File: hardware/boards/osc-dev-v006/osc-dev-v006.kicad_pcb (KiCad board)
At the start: 6 copper layers, 50 x 40 mm, 87 parts, among them J1 JST-PH-H, J10 TTL-JST, J2 LINKE, J3 Qwiic, J4 MOT, J5 POS, J6 ENC, J7 NTC, J8 TTL, J9 TTL-JST, U1 HT7533-1, U2 CH32V006F8P6, U3 DRV8212PDSGR

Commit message: board: v006 rev-2a schematic refresh, family designators, terminal bias, tier-2 position input
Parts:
- renumbered C13 to Ca1, C6 to Ch1, C7 to Ch2, C8 to Ch3, C9 to Ch4, Cin1 to Ci1, C1 to Cp1, C2 to Cp2, C3 to Cp3, C4 to Cu1, C5 to Cu2, LED1 to Dl1, LED2 to Dl2, D4 to Dl3, D5 to Dl4, D1 to Dp1, D2 to Dp2, D6 to Dx1, R21 to Ra1, R14 to Rh1, R1 to Rl1, R2 to Rl2, R4 to Rl3, R8 to Rl4, R22 to Rn1, R12 to Rq1, R13 to Rq2, R10 to Rq3, R11 to Rq4, RS1 to Rs1, RS2 to Rs2, R7 to Ru1, R23 to Rx1, R24 to Rx2

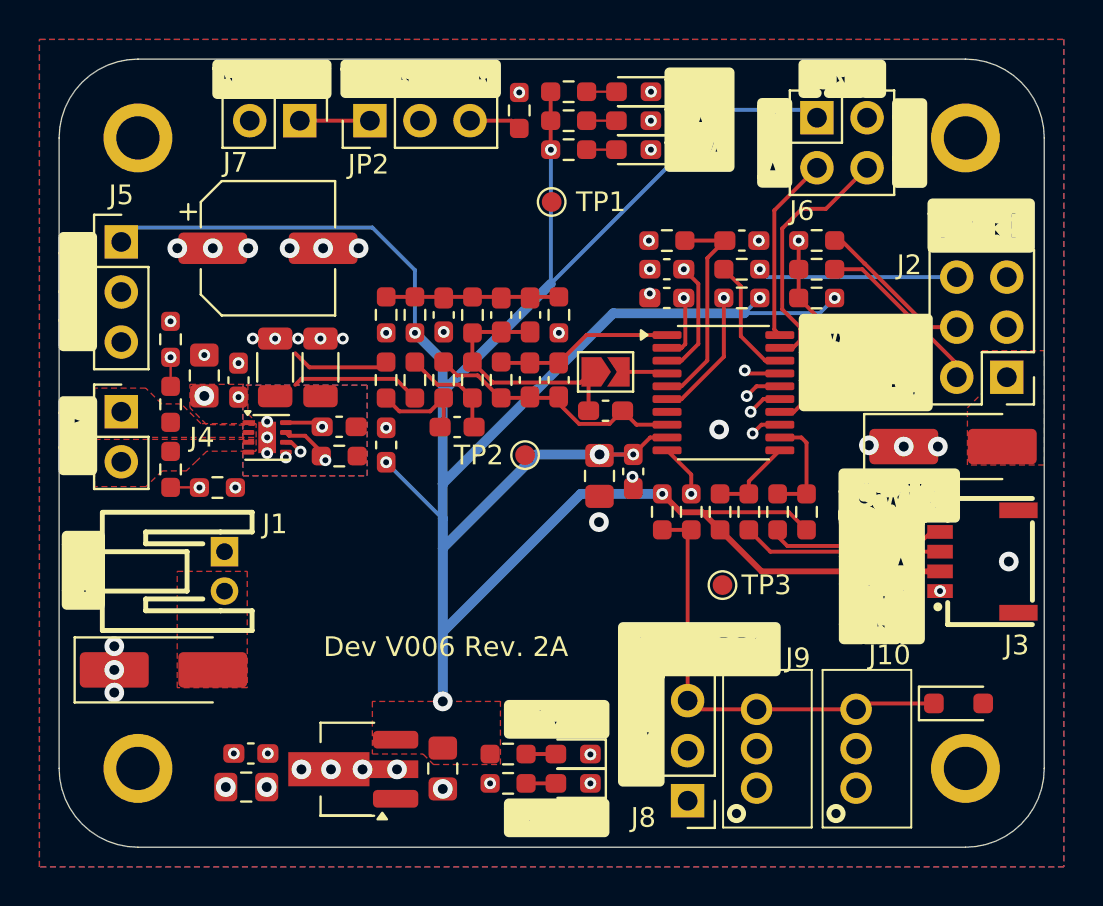
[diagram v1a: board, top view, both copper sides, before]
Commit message: board: v006 rev-2a placement, silk labels, test point rows, silk rules
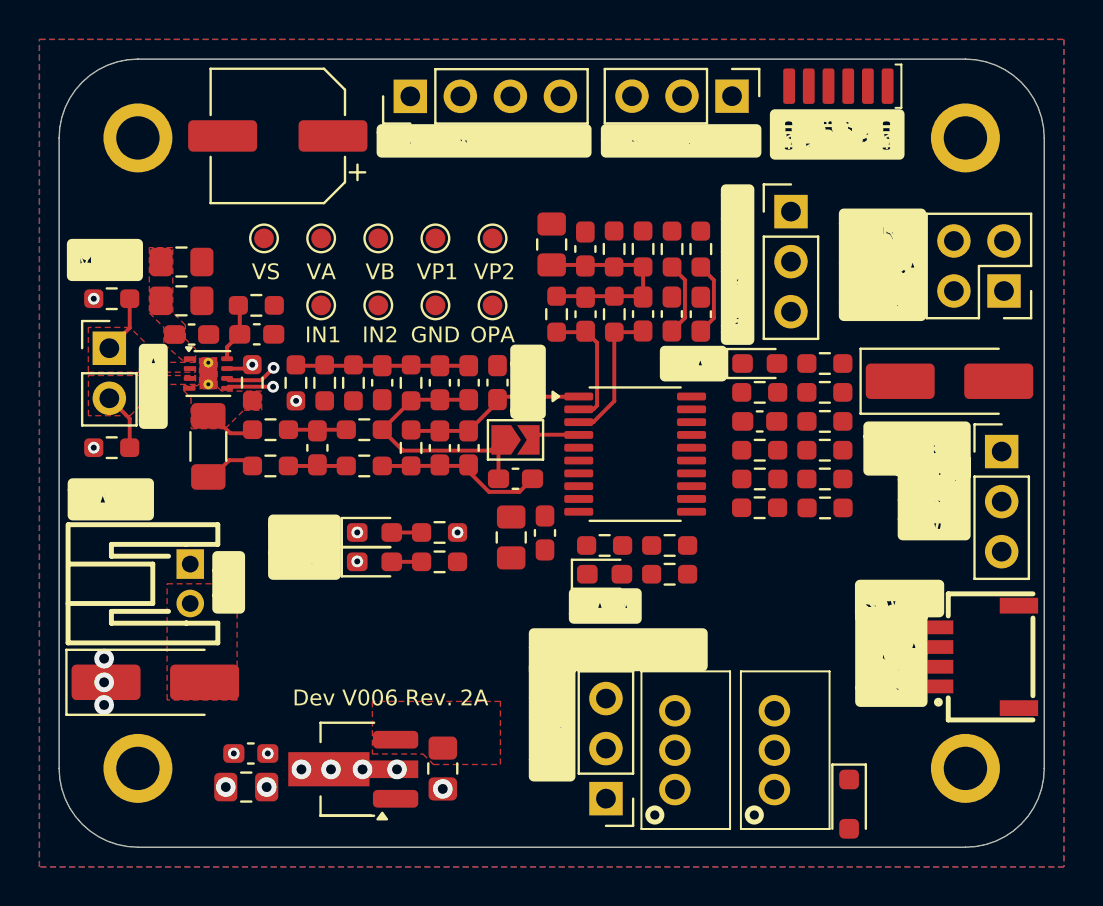
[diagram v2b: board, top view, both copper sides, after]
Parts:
- removed D3: BLUE, LED_SMD:LED_0603_1608Metric_Pad1.05x0.95mm_HandSolder
- removed FB1: 600Ω@100MHz, Inductor_SMD:L_0603_1608Metric_Pad1.05x0.95mm_HandSolder
- removed R3: 4K7, Resistor_SMD:R_0603_1608Metric_Pad0.98x0.95mm_HandSolder
- removed R5: 100, Resistor_SMD:R_0603_1608Metric_Pad0.98x0.95mm_HandSolder
- removed R6: 1K, Resistor_SMD:R_0603_1608Metric_Pad0.98x0.95mm_HandSolder
- removed R9: 10K, Resistor_SMD:R_0603_1608Metric_Pad0.98x0.95mm_HandSolder
- removed Rs2: 60m, Resistor_SMD:R_1206_3216Metric
- added Ca2: 100nF, Capacitor_SMD:C_0603_1608Metric_Pad1.08x0.95mm_HandSolder, F.Cu at (142.6, 122.9)
- added Cb1: 10uF, Capacitor_SMD:C_0805_2012Metric_Pad1.18x1.45mm_HandSolder, F.Cu at (135.0, 119.4)
- added Cb2: 100nF, Capacitor_SMD:C_0603_1608Metric_Pad1.08x0.95mm_HandSolder, F.Cu at (136.7, 119.6)
- added Ch4: 10uF, Capacitor_SMD:C_0805_2012Metric_Pad1.18x1.45mm_HandSolder, F.Cu at (116.2, 120.3)
- added Co1: 100pF, Capacitor_SMD:C_0603_1608Metric_Pad1.08x0.95mm_HandSolder, F.Cu at (132.2, 126.4)
- added Cv3: 100pF, Capacitor_SMD:C_0603_1608Metric_Pad1.08x0.95mm_HandSolder, F.Cu at (145.6, 128.4)
- added J11: Conn_01x06, shared:Flex_Landing_1x06_P1.0mm, F.Cu at (149.6, 111.4)
- added Ra2: 4K7, Resistor_SMD:R_0603_1608Metric_Pad0.98x0.95mm_HandSolder, F.Cu at (142.6, 119.6)
- added Rb1: 430, Resistor_SMD:R_0603_1608Metric_Pad0.98x0.95mm_HandSolder, F.Cu at (139.6, 119.6)
- added Rb2: 100, Resistor_SMD:R_0603_1608Metric_Pad0.98x0.95mm_HandSolder, F.Cu at (138.2, 119.6)
- added Rh2: 0R, Resistor_SMD:R_0603_1608Metric_Pad0.98x0.95mm_HandSolder, F.Cu at (120.0, 122.5)
- added Rv5: 6K4, Resistor_SMD:R_0603_1608Metric_Pad0.98x0.95mm_HandSolder, F.Cu at (148.9, 129.8)
- added Rv6: 1K6, Resistor_SMD:R_0603_1608Metric_Pad0.98x0.95mm_HandSolder, F.Cu at (145.6, 129.8)
- added TP4: IN2, TestPoint:TestPoint_Pad_D1.0mm, F.Cu at (126.2, 122.5)
- added TP5: VA, TestPoint:TestPoint_Pad_D1.0mm, F.Cu at (123.3, 119.1)
- added TP6: VB, TestPoint:TestPoint_Pad_D1.0mm, F.Cu at (126.2, 119.1)
- added TP7: VS, TestPoint:TestPoint_Pad_D1.0mm, F.Cu at (120.4, 119.1)
- added TP8: VP1, TestPoint:TestPoint_Pad_D1.0mm, F.Cu at (129.1, 119.1)
- added TP9: VP2, TestPoint:TestPoint_Pad_D1.0mm, F.Cu at (132.0, 119.1)
- Cc3, Cc4: value 47pF -> 22pF
- Ch3, Cp1, Cp3, Cu1: value 10µF -> 10uF
- Ch5: renamed from Ch4; value 100µF -> 100uF
- Cp2: value 1µF -> 1uF
- J2: footprint Connector_PinHeader_2.54mm:PinHeader_2x03_P2.54mm_Vertical -> Connector_PinHeader_2.54mm:PinHeader_1x03_P2.54mm_Vertical
- J5: footprint Connector_PinHeader_2.54mm:PinHeader_1x03_P2.54mm_Vertical -> Connector_PinHeader_2.54mm:PinHeader_1x04_P2.54mm_Vertical
- J7: footprint Connector_PinHeader_2.54mm:PinHeader_1x02_P2.54mm_Vertical -> Connector_PinHeader_2.54mm:PinHeader_1x03_P2.54mm_Vertical
- Rk1, Rk2: value 0 -> 0R
- Rs1: value 33m -> 60m; footprint Resistor_SMD:R_1206_3216Metric -> Resistor_SMD:R_1206_3216Metric_Pad1.30x1.75mm_HandSolder
- Rv1, Rv3: value 20K -> 6K4
- Rv2, Rv4: value 10K -> 1K6
- TH1: value 10kΩ 3950K -> 10K/3950
- TP2: value GND -> OPA
- TP3: value GND -> IN1
- U3: footprint Package_SON:Texas_DSG0008A_WSON-8-1EP_2x2mm_P0.5mm_EP0.9x1.6mm -> Package_SON:Texas_DSG0008A_WSON-8-1EP_2x2mm_P0.5mm_EP0.9x1.6mm_ThermalVias
- moved TP3 24.8 mm to (123.3, 122.5)
- moved Rl3 23.6 mm to (141.0, 136.1), turned to 180 degrees
- moved Dl3 23.1 mm to (137.7, 136.1), turned to 0 degrees
- moved Rv4 22.0 mm to (138.2, 122.9), turned to 90 degrees
- moved J7 22.0 mm to (144.2, 111.9)
- moved JP2 21.9 mm to (147.1, 117.7), turned to 0 degrees
- moved Rv2 19.6 mm to (135.2, 122.9)
- moved TH1 18.8 mm to (145.6, 126.9), turned to 180 degrees
- moved Rl4 16.9 mm to (148.9, 125.5), turned to 180 degrees
- moved J5 16.4 mm to (127.8, 111.9), turned to 90 degrees
- moved Dl1 16.2 mm to (126.0, 134.0), turned to 0 degrees
- moved Dl2 14.0 mm to (126.0, 135.5), turned to 0 degrees
- moved Rl1 13.2 mm to (129.3, 134.0), turned to 180 degrees
- moved J6 12.9 mm to (158.0, 121.8), turned to 180 degrees
- moved Dl4 12.6 mm to (145.6, 125.5), turned to 0 degrees
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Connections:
- net /MCU/VPOS renamed /MCU/VPOS1
- net /SENS/POT renamed /SENS/POS1
- Ch1 pad 2: PGND -> GND
- Cv1 pad 2: GND -> /SENS/VB
- Cv2 pad 2: GND -> /SENS/VB
- J2 pad 2: /MCU/TEL_TX -> GND
- J2 pad 3: GND -> /MCU/SWDIO_J
- J7 pad 2: GND -> +3V3
- JP2 pad 2: /MCU/VNTC -> /MCU/VPOS2_NTC
- Rn1 pad 2: /MCU/VNTC -> /SENS/VNTC_INT
- Rv2 pad 2: GND -> /SENS/VB
- Rv4 pad 2: GND -> /SENS/VB
- TP2 pad 1: GND -> /MCU/OPA_OUT
- TP3 pad 1: GND -> /DRV/DRV_IN1
- U2 pad 14: /MCU/TEL -> /MCU/VSNS
- U2 pad 6: /MCU/VNTC -> /MCU/VPOS2_NTC
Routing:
- net +3V3: track 153.4 -> 0.00 mm, vias 9 -> 1
- net /MCU/VSNB: track 43.9 -> 7.23 mm, vias 2 -> 1
- net /SENS/POS1: track 31.9 -> 0.00 mm, vias 1 -> 0
- net /COMMS/DATA: track 28.0 -> 0.00 mm, vias 2 -> 0
- net /MCU/VNTC: track 26.2 -> 0.00 mm, vias 1 -> 0
- net /MCU/VSNA: track 32.4 -> 6.51 mm, vias 2 -> 1
- net /DRV/DRV_EN: track 27.1 -> 1.36 mm, vias 2 -> 1
- net /DRV/DRV_IN2: track 27.0 -> 2.37 mm, vias 2 -> 1
- net /DRV/DRV_IN1: track 26.6 -> 2.66 mm, vias 2 -> 1
- net /COMMS/DATA_J: track 23.0 -> 0.00 mm
- net /MCU/TEL: track 21.0 -> 0.00 mm, vias 2 -> 0
- net /MCU/STAT: track 15.0 -> 0.00 mm, vias 2 -> 0
- net /MCU/ENCB: track 12.8 -> 0.00 mm
- net /SENS/VB: track 0.00 -> 10.6 mm
- net /MCU/SDA_J: track 10.2 -> 0.00 mm
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- removed copper zone on B.Cu, net PGND
- removed copper zone on F.Cu, net VPROG
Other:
- board text added: "+5V"
- board text added: "BATT"
- board text added: "BOOT"
- board text added: "DATA"
- board text added: "IN1"
- board text added: "IN2"
- board text added: "MOT"
- board text added: "OPA"
- board text added: "OSC BUS"
- board text added: "P1"
- board text added: "P2"
- board text added: "QA"
- board text added: "QB"
- board text added: "STAT"
- board text added: "VA"
- board text added: "VB"
- board text added: "VP1"
- board text added: "VP2"
- board text added: "VS"
- board text removed: "3"
- board text removed: "3 G P"
- board text removed: "5V"
- board text removed: "A"
- board text removed: "B"
- board text removed: "DAT"
- board text removed: "NTC_EX"
- board text removed: "OSC TTL"
- board text removed: "RX"
- board text removed: "STA"
- board text removed: "TEL"
- board text removed: "TX"

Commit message: board: v006 rev-2a routed, power tree, test point rows
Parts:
- moved TP7 32.8 mm to (148.9, 135.4)
- moved TP2 4.92 mm to (134.1, 127.0)
- moved TP5 3.40 mm to (123.3, 122.5)
- moved TP6 3.40 mm to (126.2, 122.5)
- moved TP3 3.30 mm to (123.3, 119.2)
- moved TP4 3.30 mm to (126.2, 119.2)
- moved Dx1 0.70 mm to (150.1, 147.1)
- turned Rv3 to 0 degrees
- turned Ch5 to 0 degrees
- turned Rv1 to 0 degrees
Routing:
- net +3V3: track 0.00 -> 167.5 mm, vias 1 -> 16
- net /DRV/DRV_IN2: track 2.37 -> 37.3 mm, vias 1 -> 3
- net /MCU/VSNB: track 7.23 -> 39.3 mm, vias 1 -> 3
- net /MCU/ENCA: track 0.00 -> 31.3 mm, vias 0 -> 1
- net /DRV/DRV_IN1: track 2.66 -> 33.5 mm, vias 1 -> 3
- net /MCU/ENCB: track 0.00 -> 29.1 mm, vias 0 -> 1
- net /DRV/DRV_EN: track 1.36 -> 28.8 mm, vias 1 -> 2
- net /MCU/VPOS2_NTC: track 3.81 -> 29.2 mm
- net /MCU/VSNA: track 6.51 -> 30.2 mm, vias 1 -> 3
- net /COMMS/DATA_J: track 0.00 -> 23.3 mm
- net /MCU/VPOS1: track 3.79 -> 26.1 mm
- net /MCU/VSNS: track 0.00 -> 13.9 mm
- net /SENS/POS1: track 0.00 -> 11.4 mm
- net /MCU/SWDIO_J: track 0.00 -> 10.8 mm
- net /SENS/VNTC_EXT: track 0.00 -> 10.3 mm
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- added copper zone on B.Cu, net +3V3
- added copper zone on F.Cu, net VPROG

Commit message: board: v006 rev-2a reroute to 0.2 mm clearance, dru floors, silk label alignment
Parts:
- moved Rh1 0.70 mm to (120.5, 126.4)
- moved Cb1 0.50 mm to (134.5, 119.4)
- moved Rq2 0.50 mm to (145.6, 133.3)
- moved Rq4 0.50 mm to (148.9, 133.3)
- moved Rv2 0.50 mm to (134.7, 122.9)
- moved Cb2 0.40 mm to (136.3, 119.6)
- moved Cv1 0.40 mm to (136.3, 122.9)
- moved Rq1 0.40 mm to (145.6, 131.7)
- moved Rq3 0.40 mm to (148.9, 131.7)
- moved Rb2 0.30 mm to (137.9, 119.6)
- moved Rv5 0.30 mm to (148.9, 130.2)
- moved Rv6 0.30 mm to (145.6, 130.2)
- moved Rv4 0.30 mm to (137.9, 122.9)
- moved Cv3 0.20 mm to (145.6, 128.6)
- moved Ru1 0.20 mm to (148.9, 128.6)
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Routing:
- net /DRV/DRV_IN2: track 37.3 -> 39.0 mm
- net /DRV/DRV_IN1: track 33.5 -> 35.0 mm
- net /MCU/ENCA: track 31.3 -> 31.8 mm
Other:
- board text added: "DAT"
- board text added: "VSY"
- board text removed: "D"
- board text removed: "V"
- board text removed: "VSYS"
